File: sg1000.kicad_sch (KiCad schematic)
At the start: 66 parts, among them CN1 Conn_01x07_Female, J1 USB-B1HSB6, J2 RCJ-014, J3 RCJ-013, Q1 2n4401, Q1c1 2n3906, SW1 Pause Key, SW2 Power Toggle, U1 SG-1000-Cart, U10 PLCCZ80, U100 74HCT574, U101 74HCT574, U102 74HCT574, U103 AS6C62256-DIP, U11 AS6C62256-DIP, U12 TMS9918A, U13 74LS139, U16 74LS32, U18 74LS257, U2 SG-1000-Expansion, U21 74LS257, U3 SN76489AN, U99 74HCT04, X2 10.73863MHz

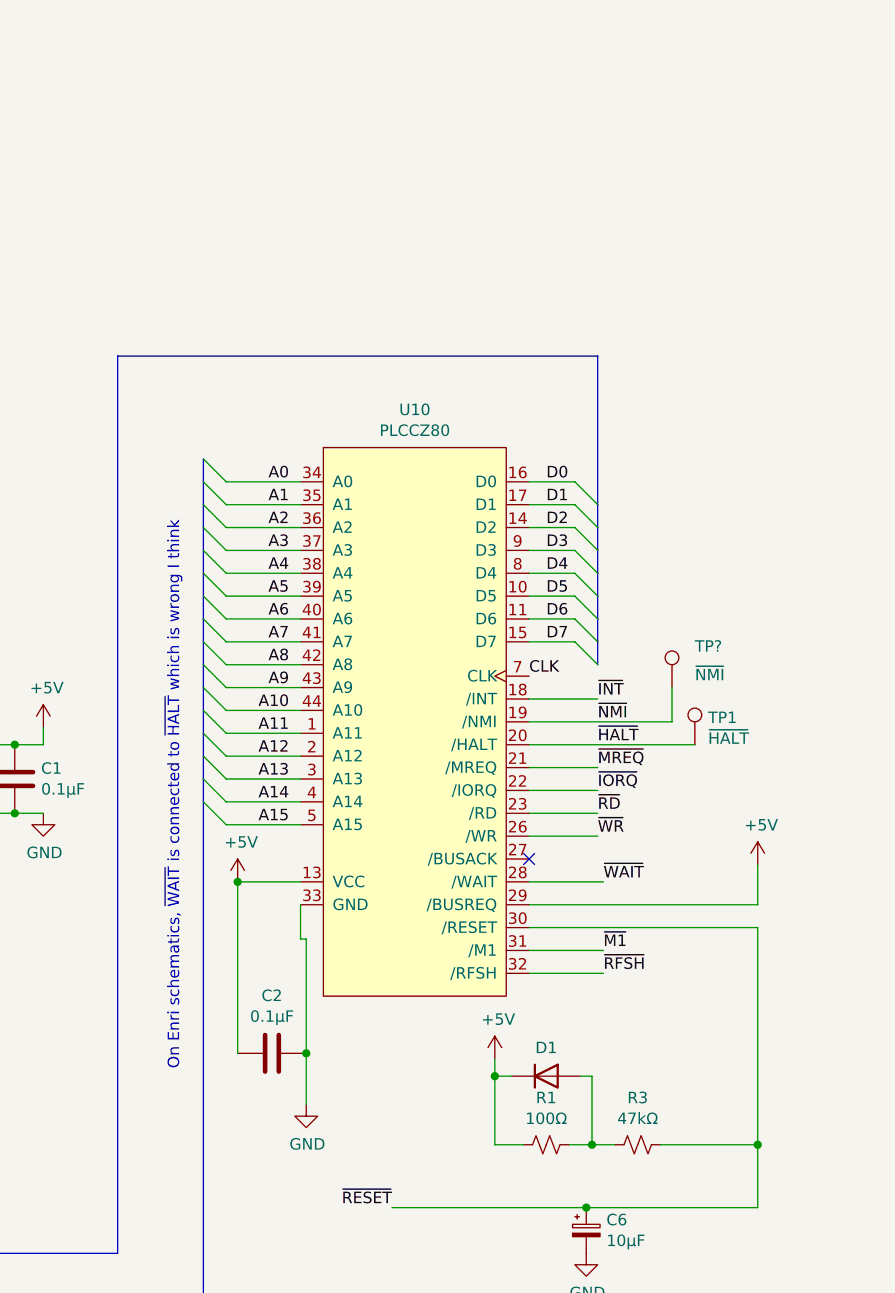
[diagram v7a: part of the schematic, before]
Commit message: /HALT is an error
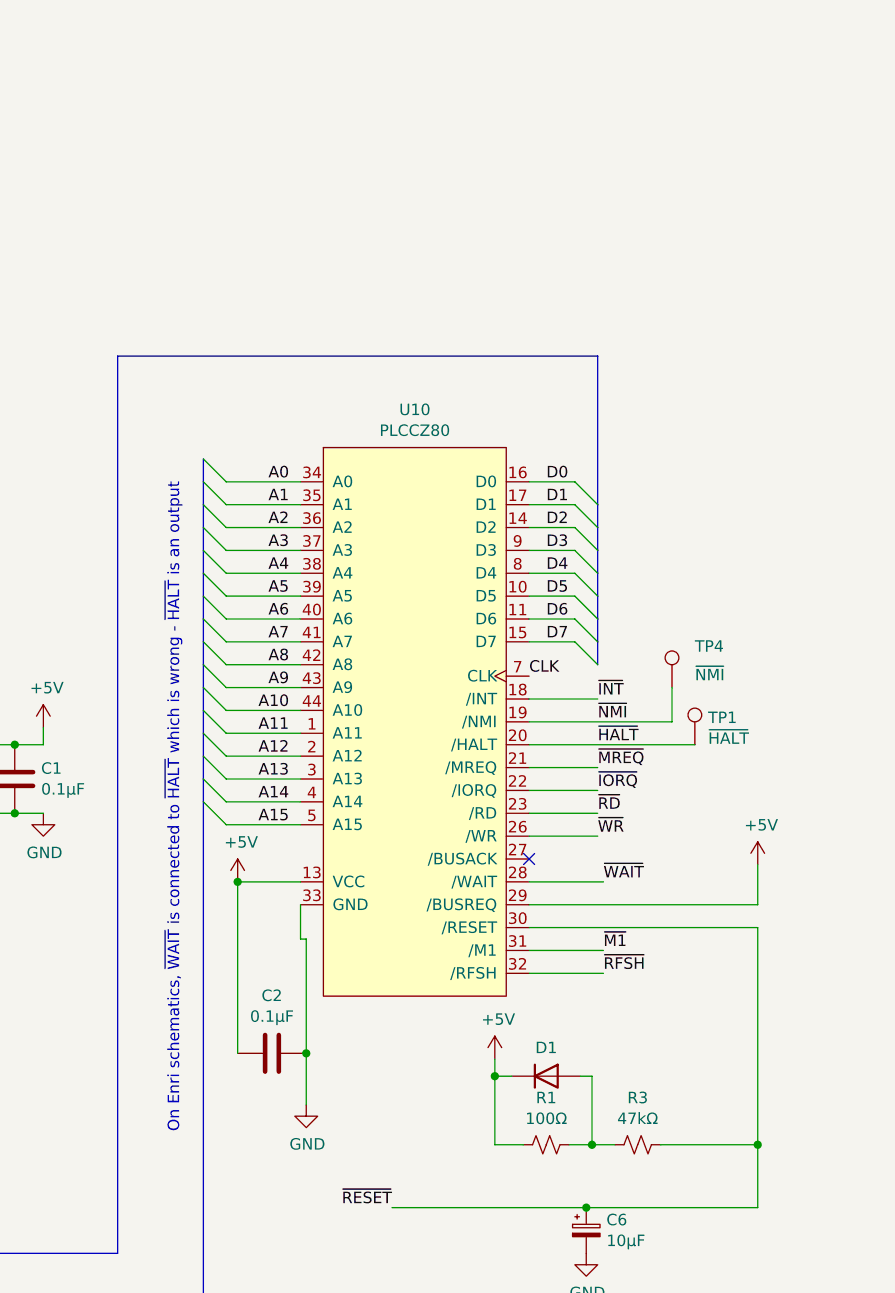
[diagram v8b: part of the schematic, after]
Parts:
- gave numbers to parts that had none: 1
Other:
- note added: "On Enri schematics, ~{WAIT} is connected to ~{HALT} which is wrong - ~{HALT} is an output"
- note removed: "On Enri schematics, ~{WAIT} is connected to ~{HALT} which is wrong I think"
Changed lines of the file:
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@@
     (effects (font (size 1.27 1.27)) (justify left bottom))
   )
-  (text "On Enri schematics, ~{WAIT} is connected to ~{HALT} which is wrong I think"
-    (at 209.55 130.175 90)
+  (text "On Enri schematics, ~{WAIT} is connected to ~{HALT} which is wrong - ~{HALT} is an output"
+    (at 209.55 137.16 90)
     (effects (font (size 1.27 1.27)) (justify left bottom))
   )
@@
   (symbol (lib_id "Connector:TestPoint") (at 264.16 87.63 0) (unit 1)
     (in_bom yes) (on_board yes) (fields_autoplaced)
-    (property "Reference" "TP?" (id 0) (at 266.7 83.0579 0)
+    (property "Reference" "TP4" (id 0) (at 266.7 83.0579 0)
       (effects (font (size 1.27 1.27)) (justify left))
     )
@@
     )
     (path "/b71eafdc-9c03-445b-8de6-c72ccf90805a"
-      (reference "TP?") (unit 1) (value "~{NMI}") (footprint "TestPoint:TestPoint_Pad_1.0x1.0mm")
+      (reference "TP4") (unit 1) (value "~{NMI}") (footprint "TestPoint:TestPoint_Pad_1.0x1.0mm")
     )
     (path "/e4e9a9cd-894c-43a6-bbd2-9190e99d71d4"
